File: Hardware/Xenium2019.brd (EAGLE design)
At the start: 39.4 x 36.2 mm, 20 parts, among them J1 SM10B-SRSS-TB, Q1 310mA/60V/1.6Ω, Q2 310mA/60V/1.6Ω, Q3 310mA/60V/1.6Ω, Q4 310mA/60V/1.6Ω, U1 XC9572XL-10VQG64, U2 AM29LV160M

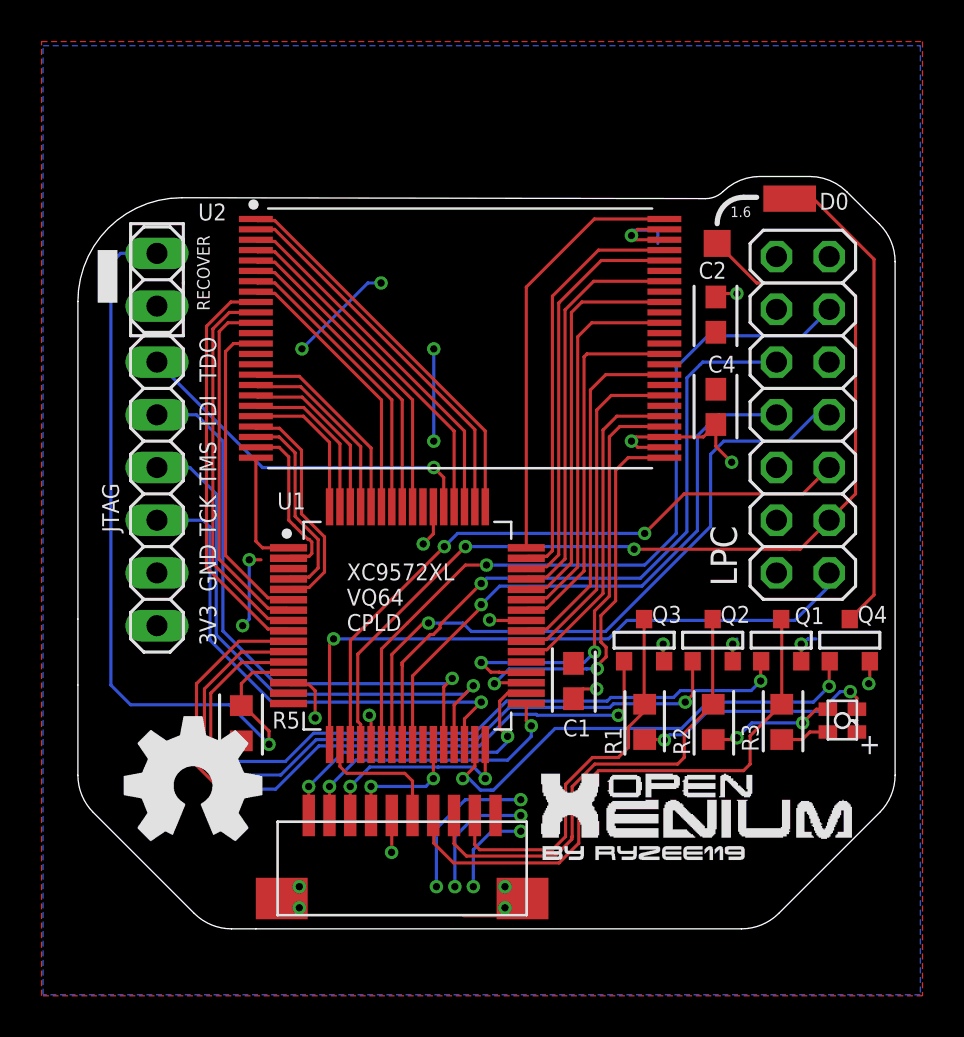
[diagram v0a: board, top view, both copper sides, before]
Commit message: Straighten out top edge of PCB
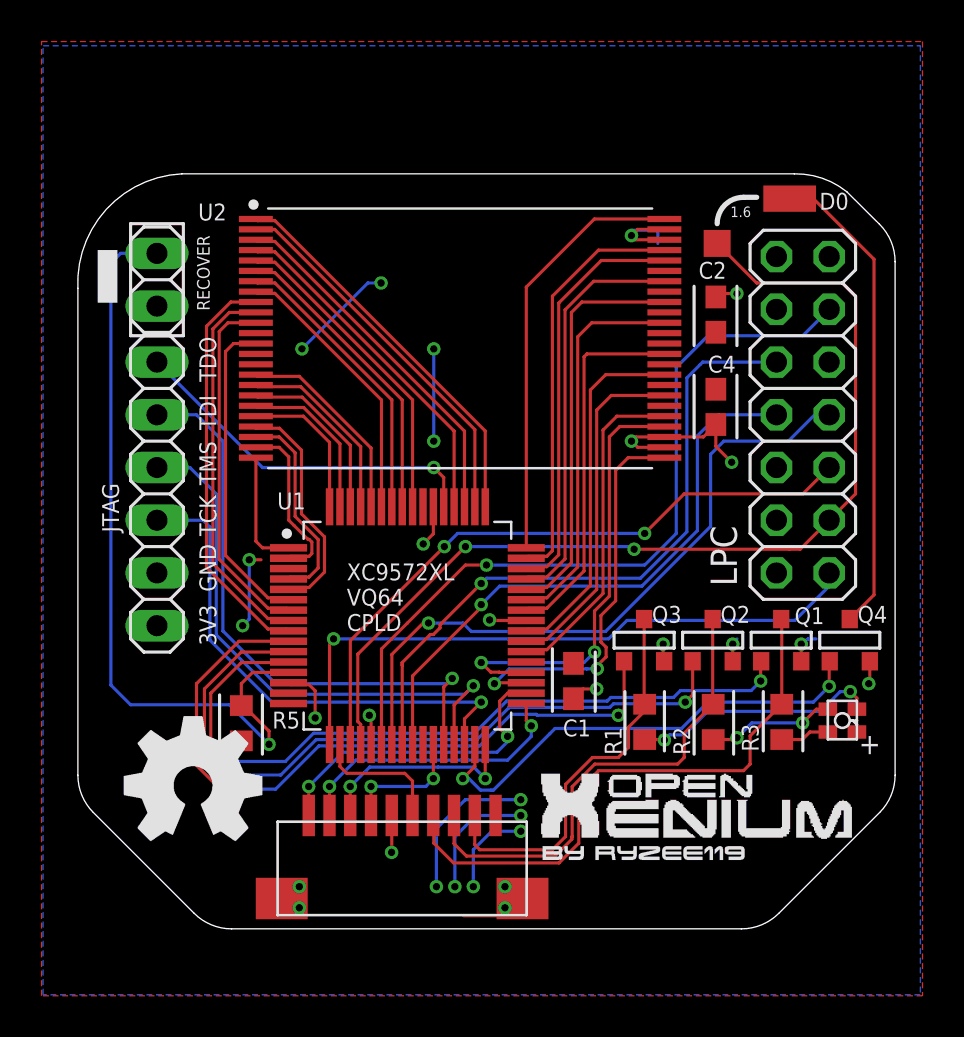
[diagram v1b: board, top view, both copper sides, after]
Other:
- board size 39.4 x 36.2 mm -> 39.4 x 36.4 mm
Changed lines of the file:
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@@
 <fusionsync huburn="a.cGVyc29uYWw6dWUyZDg2Yzlk" projecturn="a.cGVyc29uYWw6dWUyZDg2YzlkIzIwMTgwNzAyMTM4NDcwMzgx" f3durn="urn:adsk.wipprod:dm.lineage:oZWMRtxXSt2iMP7dGeI6xg" pcbguid="fe7e8d9e-3715-4ad1-9c8f-f34774275f9c" lastpulledtime="" lastsyncedchangeguid="37ddcd76-2083-5299-7c1b-71ff94e5e9aa"/>
 <plain>
-<wire x1="30.697896875" y1="0" x2="7.3025" y2="0" width="0" layer="20"/>
+<wire x1="30.697896875" y1="0" x2="6.132103125" y2="0" width="0" layer="20"/>
 <wire x1="30.697896875" y1="0" x2="32.49395" y2="0.74395" width="0" layer="20" curve="45.00005"/>
 <wire x1="32.49395" y1="0.74395" x2="37.35605" y2="5.60605" width="0" layer="20"/>
@@
 <wire x1="38.1" y1="32.141028125" x2="37.35016875" y2="33.94294375" width="0" layer="20" curve="45.187369"/>
 <wire x1="37.35016875" y1="33.94294375" x2="35.774928125" y2="35.507915625" width="0" layer="20"/>
-<wire x1="35.774928125" y1="35.507915625" x2="33.984759375" y2="36.246" width="0" layer="20" curve="44.812631"/>
-<wire x1="33.984759375" y1="36.246" x2="31.590915625" y2="36.246" width="0" layer="20"/>
-<wire x1="31.590915625" y1="36.246" x2="29.81578125" y2="35.522728125" width="0" layer="20" curve="44.336545"/>
-<wire x1="29.81578125" y1="35.522728125" x2="28.97216875" y2="35.179815625" width="0" layer="20" curve="-44.431599"/>
-<wire x1="28.97216875" y1="35.179815625" x2="3.738296875" y2="35.221690625" width="0" layer="20"/>
-<wire x1="3.738296875" y1="35.221690625" x2="-1.27" y2="30.221696875" width="0" layer="20" curve="90.095864"/>
-<wire x1="-1.27" y1="30.221696875" x2="-1.27" y2="14.9225" width="0" layer="20"/>
+<wire x1="35.774928125" y1="35.507915625" x2="33.2486" y2="36.3728" width="0" layer="20" curve="40"/>
+<wire x1="3.738296875" y1="36.3728" x2="-1.27" y2="30.856696875" width="0" layer="20" curve="90.095864"/>
+<wire x1="-1.27" y1="30.856696875" x2="-1.27" y2="7.402103125" width="0" layer="20"/>
 <text x="5.3975" y="13.6525" size="0.8128" layer="21" font="vector" rot="R90">3V3</text>
 <text x="5.3975" y="16.239084375" size="0.8128" layer="21" font="vector" rot="R90">GND</text>
@@
 <rectangle x1="-0.3175" y1="30.1625" x2="0.635" y2="32.7025" layer="21"/>
 <text x="5.08" y="29.7815" size="0.6096" layer="21" font="vector" rot="R90">RECOVER</text>
-<wire x1="-1.27" y1="14.9225" x2="-1.27" y2="11.7475" width="0" layer="20"/>
-<wire x1="-1.27" y1="7.402103125" x2="-1.27" y2="11.7475" width="0" layer="20"/>
 <wire x1="6.132103125" y1="0" x2="4.33605" y2="0.74395" width="0" layer="20" curve="-45.00005"/>
 <wire x1="4.33605" y1="0.74395" x2="-0.52605" y2="5.60605" width="0" layer="20"/>
 <wire x1="-0.52605" y1="5.60605" x2="-1.27" y2="7.402103125" width="0" layer="20" curve="-45.00007"/>
-<wire x1="7.3025" y1="0" x2="6.132103125" y2="0" width="0" layer="20"/>
 <rectangle x1="2.231390625" y1="4.22275" x2="2.266946875" y2="4.24053125" layer="21"/>
 <rectangle x1="6.303009375" y1="4.22275" x2="6.320790625" y2="4.24053125" layer="21"/>
@@
 <text x="30.1625" y="34.29" size="0.508" layer="21" font="vector" ratio="12">1.6</text>
 <wire x1="1.27" y1="33.9725" x2="3.81" y2="33.9725" width="0.1524" layer="21"/>
-<wire x1="3.81" y1="33.9725" x2="3.81" y2="31.115" width="0.1524" layer="21"/>
-<wire x1="3.81" y1="31.115" x2="3.81" y2="28.575" width="0.1524" layer="21"/>
+<wire x1="3.81" y1="33.9725" x2="3.81" y2="28.575" width="0.1524" layer="21"/>
 <wire x1="3.81" y1="28.575" x2="1.27" y2="28.575" width="0.1524" layer="21"/>
 <wire x1="1.27" y1="28.575" x2="1.27" y2="33.9725" width="0.1524" layer="21"/>
@@
 <wire x1="23.65375" y1="13.335" x2="23.65375" y2="10.4775" width="0.1524" layer="21"/>
 <text x="36.35375" y="8.41375" size="1.016" layer="21">+</text>
+<wire x1="33.2486" y1="36.3728" x2="3.738296875" y2="36.3728" width="0" layer="20"/>
 </plain>
 <attributes>
